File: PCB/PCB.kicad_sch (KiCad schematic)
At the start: 2 parts, among them U1 ESP32-DevKitC

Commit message: PCB progress
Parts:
- added BT1: Battery_Cell, Connector_PinHeader_2.54mm:PinHeader_1x02_P2.54mm_Vertical, symbol Device:Battery_Cell
- added D1: D, Diode_THT:D_A-405_P10.16mm_Horizontal, symbol Device:D
- added J1, J2, J3: Conn_01x04_Pin, Connector_PinHeader_2.54mm:PinHeader_1x04_P2.54mm_Vertical, symbol Connector:Conn_01x04_Pin
- added R1: 12k, Resistor_THT:R_Axial_DIN0207_L6.3mm_D2.5mm_P10.16mm_Horizontal, symbol Device:R
- added R2: 22k, Resistor_THT:R_Axial_DIN0207_L6.3mm_D2.5mm_P10.16mm_Horizontal, symbol Device:R
- added R3, R4, R5: 10k, Resistor_SMD:R_0402_1005Metric, symbol Device:R_Small
- added SW1: SW_SPDT, Connector_PinHeader_2.54mm:PinHeader_1x03_P2.54mm_Vertical, symbol Switch:SW_SPDT
- added SW2: SW_Push, Button_Switch_THT:SW_PUSH-12mm, symbol Switch:SW_Push
- added U2: ~, charging_module:TP4056-18650, symbol charging_module:charging_module
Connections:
- net +3.3V: now also DWM1.5 (VCC), J1.2 (Pin_2); no longer DWM1.15 (VCC)
- net CLK: now also DWM1.9 (SCK); no longer DWM1.23 (VSS)
- net CS: now also DWM1.12 (NSS); no longer DWM1.26 (NSS)
- net GND: now also DWM1.20 (GND), DWM1.6 (GND), DWM1.8 (GND), J1.1 (Pin_1), J3.4 (Pin_4), R2.2, SW2.1, U2.2 (GND), U2.3 (GND); no longer DWM1.16 (VSS), DWM1.22 (GND), DWM1.38 (GND)
- net MISO: now also DWM1.10 (MISO); no longer DWM1.24 (VSS)
- net MOSI: now also DWM1.11 (MOSI); no longer DWM1.25 (MOSI)
- net RST: now also DWM1.3 (~{RSTn}), U1.27 (GPIO16); no longer U1.29 (GPIO5)
- net at U1.19 (5V): now also SW1.3 (C)
- net IRQ: now reaches U1.28 (GPIO17)
- net IRQ: now also DWM1.7 (~{IRQn})
- net GPIO18: now reaches U1.30 (GPIO18)
- net GPIO18: now also J2.2 (Pin_2)
- net GPIO19: now reaches U1.31 (GPIO19)
- net GPIO19: now also J2.3 (Pin_3)
- net SDA: now reaches U1.33 (GPIO21)
- net SDA: now also J1.3 (Pin_3)
- net SCL: now reaches U1.36 (GPIO22)
- net SCL: now also J1.4 (Pin_4)
- net GPIO23: now reaches U1.37 (GPIO23)
- net GPIO23: now also J2.4 (Pin_4)
- net at U1.7 (32K_XP/GPIO32/ADC1_CH4): now also SW2.2
- net VBAT: now reaches U1.8 (32K_XN/GPIO33/ADC1_CH5)
- net VBAT: now also R1.2, R2.1
- new net: BT1.2 (-), U2.4 (B-)
- new net: BT1.1 (+), U2.5 (B+)
- new net: D1.2 (A), R1.1, U2.6 (VOUT)
- new net: DWM1.16 (VSS), R3.1
- new net: J3.1 (Pin_1), R3.2
- new net: J3.2 (Pin_2), R4.2
- new net: J3.3 (Pin_3), R5.2
- new net: DWM1.17 (GPIO2), R4.1
- new net: DWM1.19 (GPIO0), R5.1
- new net +5V: D1.1 (K), SW1.2 (B)
- new net GPIO5: J2.1 (Pin_1), U1.29 (GPIO5)
- now unconnected: DWM1.16 (VSS)
- no-connect marks 0 -> 9
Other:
- moved on the sheet: DWM1

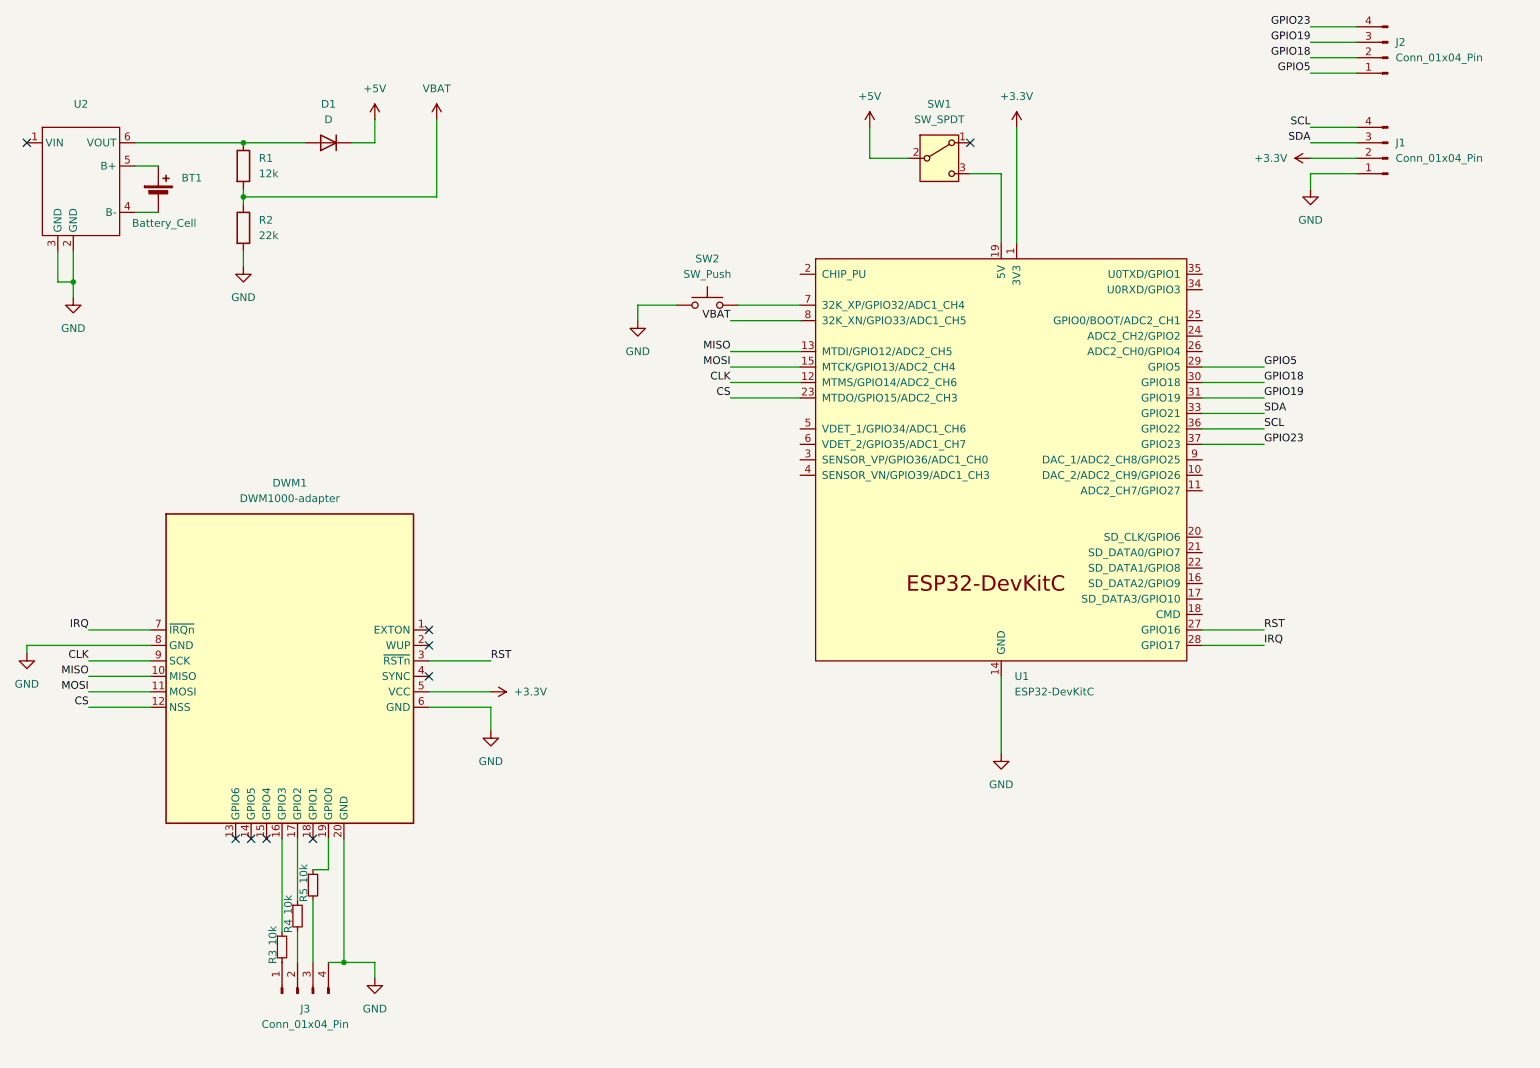
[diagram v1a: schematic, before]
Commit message: PCB is finished, but esp is the wrong way :(
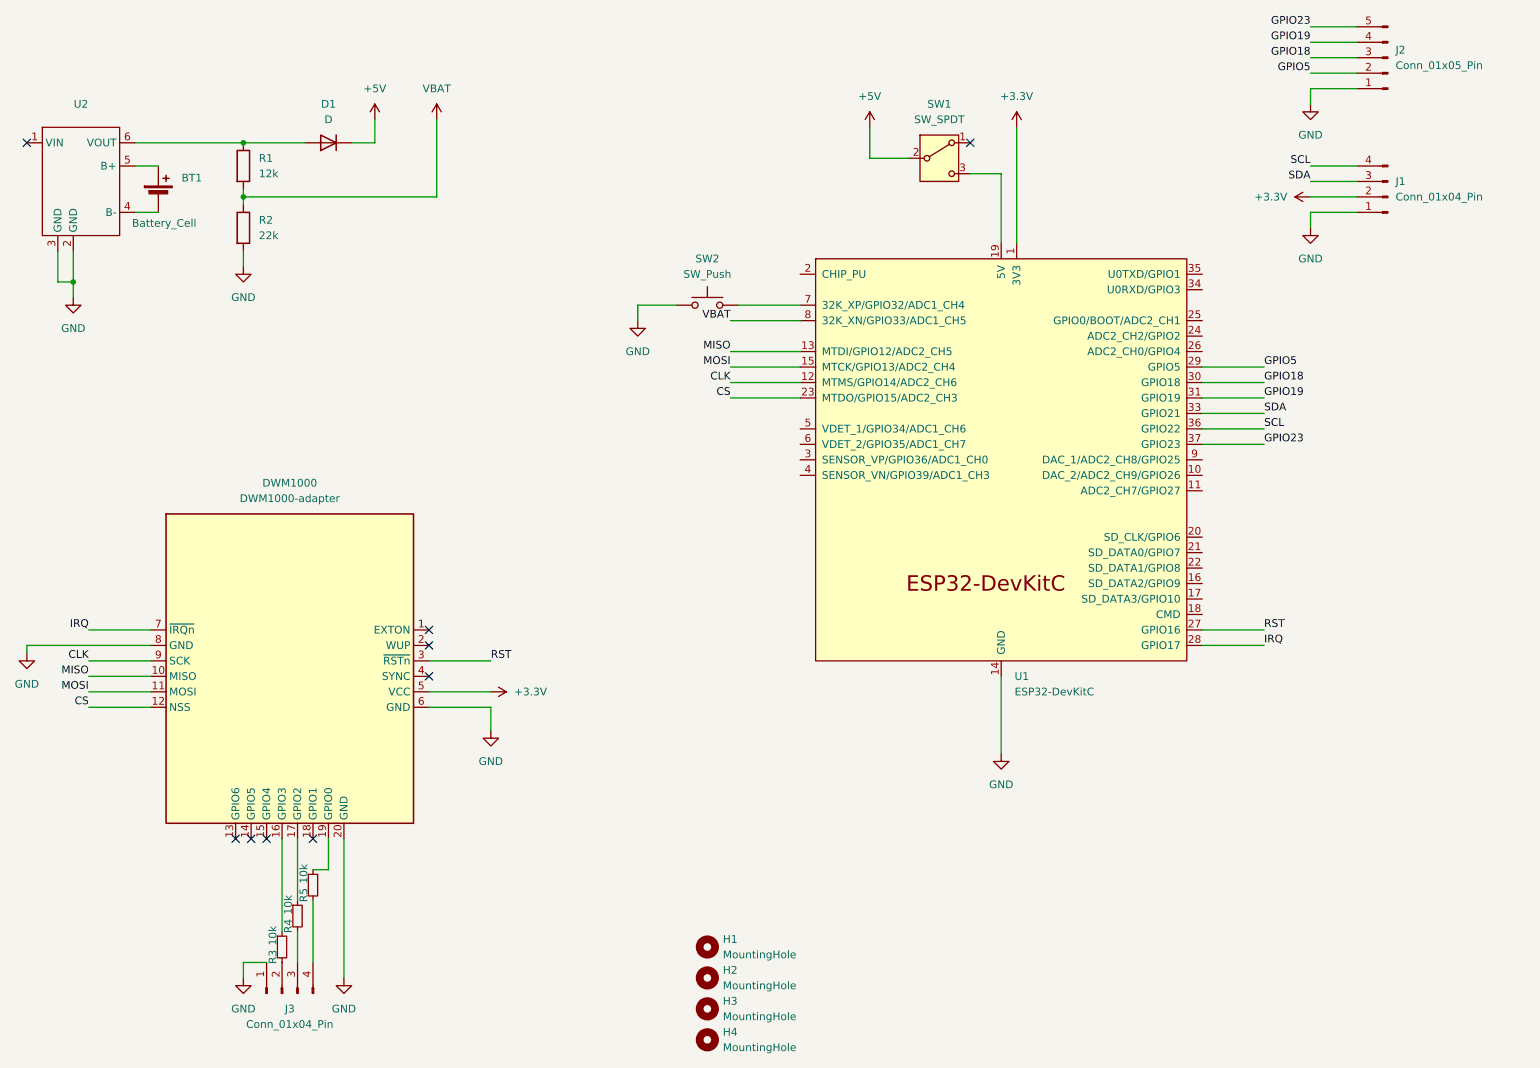
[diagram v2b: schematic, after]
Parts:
- removed J2: Conn_01x04_Pin, Connector_PinHeader_2.54mm:PinHeader_1x04_P2.54mm_Vertical, symbol Connector:Conn_01x04_Pin
- added H1, H2, H3, H4: MountingHole, MountingHole:MountingHole_4.3mm_M4, symbol Mechanical:MountingHole
- added J2: Conn_01x05_Pin, Connector_PinHeader_2.54mm:PinHeader_1x05_P2.54mm_Vertical, symbol Connector:Conn_01x05_Pin
- renumbered DWM1 to DWM1000
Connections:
- net GND: now also J3.1 (Pin_1), J2.1 (Pin_1); no longer J3.4 (Pin_4)
- net GPIO18: now also J2.3 (Pin_3)
- net GPIO19: now also J2.4 (Pin_4)
- net GPIO23: now also J2.5 (Pin_5)
- net GPIO5: now also J2.2 (Pin_2)
- net at R3.2: now also J3.2 (Pin_2); no longer J3.1 (Pin_1)
- net at R4.2: now also J3.3 (Pin_3); no longer J3.2 (Pin_2)
- net at R5.2: now also J3.4 (Pin_4); no longer J3.3 (Pin_3)
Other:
- moved on the sheet: J1, J3

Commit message: PCB redesign
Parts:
- H1, H2, H3, H4: footprint MountingHole:MountingHole_4.3mm_M4 -> MountingHole:MountingHole_3.2mm_M3
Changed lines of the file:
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@@
+	(wire
+		(pts
+			(xy 196.85 52.07) (xy 196.85 40.64)
+		)
+		(stroke
+			(width 0)
+			(type default)
+		)
+	)
 	(wire
 		(pts
@@
 	(wire
 		(pts
+			(xy 196.85 40.64) (xy 191.77 40.64)
+		)
+		(stroke
+			(width 0)
+			(type default)
+		)
+	)
+	(wire
+		(pts
 			(xy 72.39 35.56) (xy 82.55 35.56)
 		)
@@
 	(wire
 		(pts
-			(xy 196.85 40.64) (xy 196.85 52.07)
-		)
-		(stroke
-			(width 0)
-			(type default)
-		)
-	)
-	(wire
-		(pts
 			(xy 229.87 82.55) (xy 240.03 82.55)
 		)
@@
 		(pts
 			(xy 90.17 35.56) (xy 93.98 35.56)
-		)
-		(stroke
-			(width 0)
-			(type default)
-		)
-	)
-	(wire
-		(pts
-			(xy 191.77 40.64) (xy 196.85 40.64)
 		)
 		(stroke
@@
 			)
 		)
-		(property "Footprint" "MountingHole:MountingHole_4.3mm_M4"
+		(property "Footprint" "MountingHole:MountingHole_3.2mm_M3"
 			(at 148.59 177.8 0)
 			(effects
@@
 			)
 		)
-		(property "Footprint" "MountingHole:MountingHole_4.3mm_M4"
+		(property "Footprint" "MountingHole:MountingHole_3.2mm_M3"
 			(at 148.59 172.72 0)
 			(effects
@@
 			)
 		)
-		(property "Footprint" "MountingHole:MountingHole_4.3mm_M4"
+		(property "Footprint" "MountingHole:MountingHole_3.2mm_M3"
 			(at 148.59 182.88 0)
 			(effects
@@
 			)
 		)
-		(property "Footprint" "MountingHole:MountingHole_4.3mm_M4"
+		(property "Footprint" "MountingHole:MountingHole_3.2mm_M3"
 			(at 148.59 167.64 0)
 			(effects

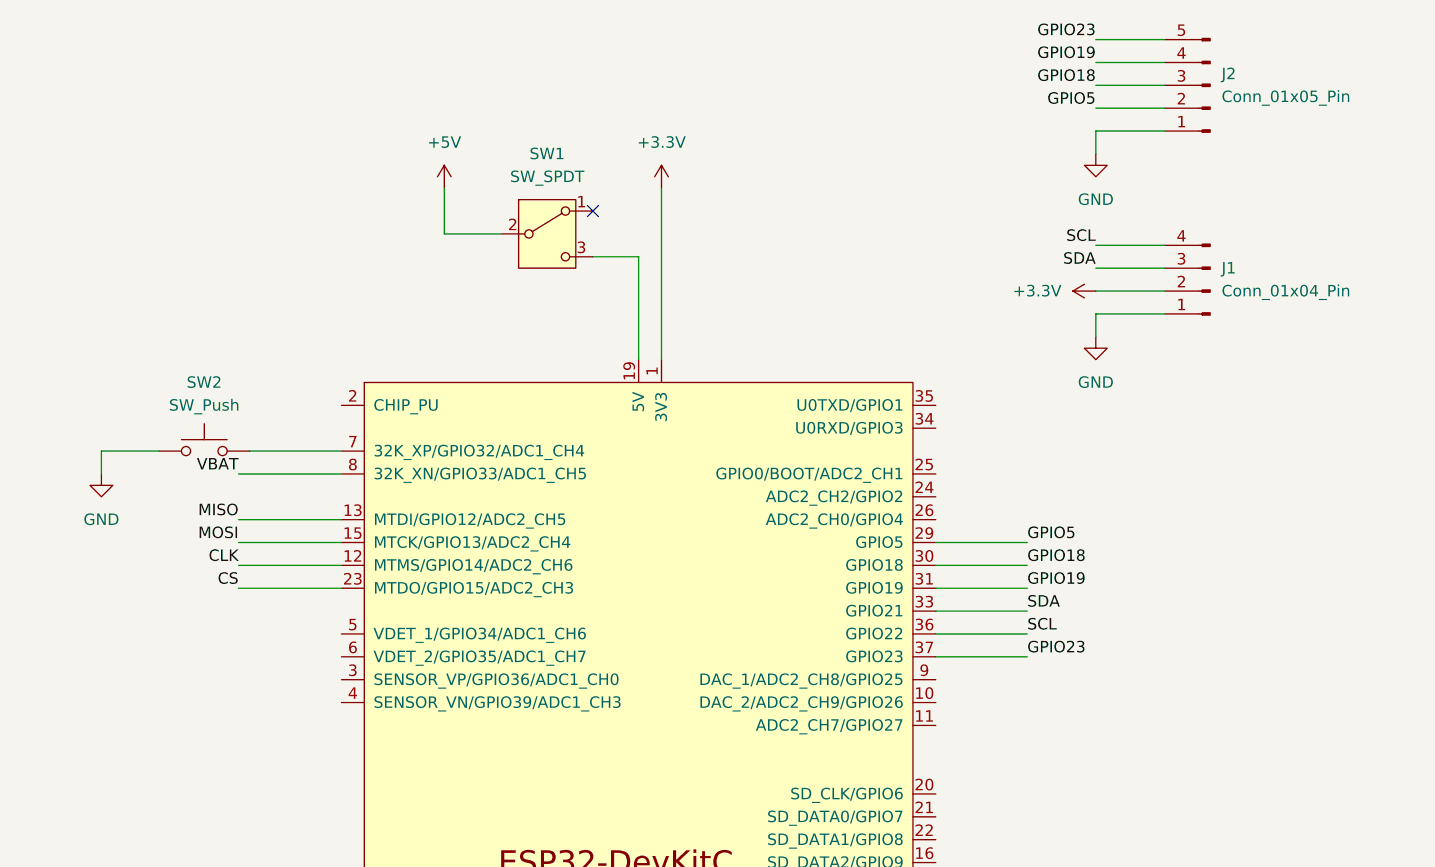
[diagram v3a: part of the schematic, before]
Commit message: added pins for motor encoders
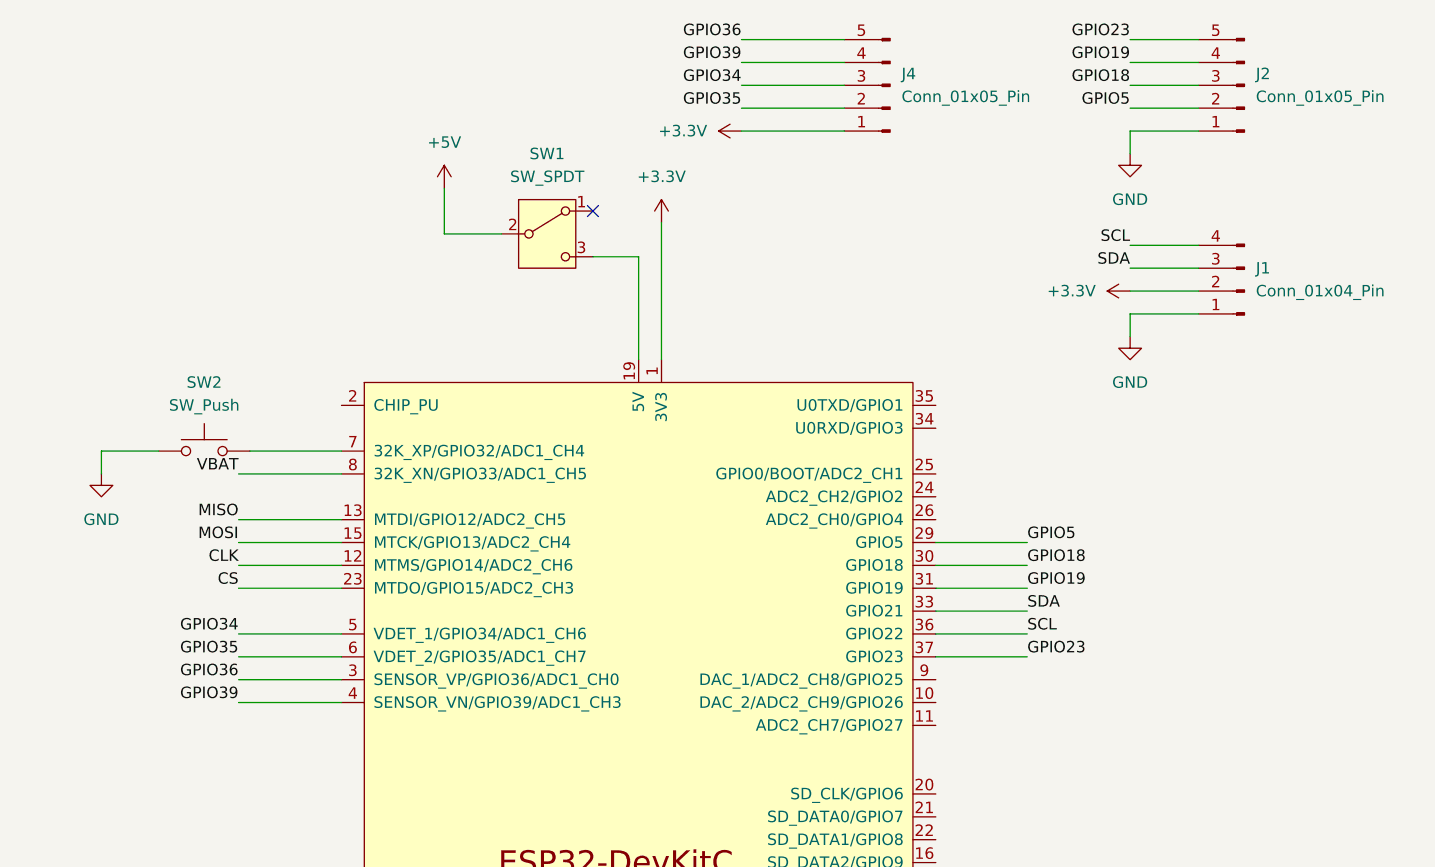
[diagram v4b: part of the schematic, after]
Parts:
- added J4: Conn_01x05_Pin, Connector_PinHeader_2.54mm:PinHeader_1x05_P2.54mm_Vertical, symbol Connector:Conn_01x05_Pin
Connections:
- net +3.3V: now also J4.1 (Pin_1)
- net GPIO36: now reaches U1.3 (SENSOR_VP/GPIO36/ADC1_CH0)
- net GPIO36: now also J4.5 (Pin_5)
- net GPIO39: now reaches U1.4 (SENSOR_VN/GPIO39/ADC1_CH3)
- net GPIO39: now also J4.4 (Pin_4)
- net GPIO34: now reaches U1.5 (VDET_1/GPIO34/ADC1_CH6)
- net GPIO34: now also J4.3 (Pin_3)
- net GPIO35: now reaches U1.6 (VDET_2/GPIO35/ADC1_CH7)
- net GPIO35: now also J4.2 (Pin_2)
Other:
- moved on the sheet: J1, J2

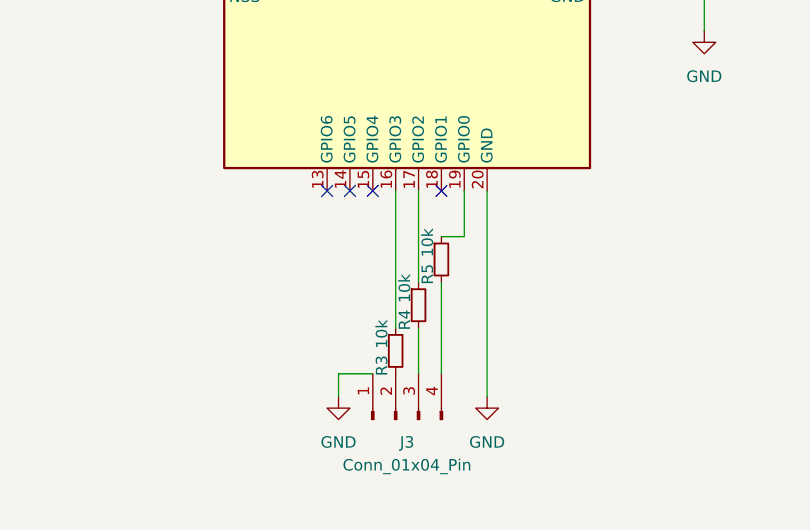
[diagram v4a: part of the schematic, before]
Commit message: new header for encoders, adjusted resitor values
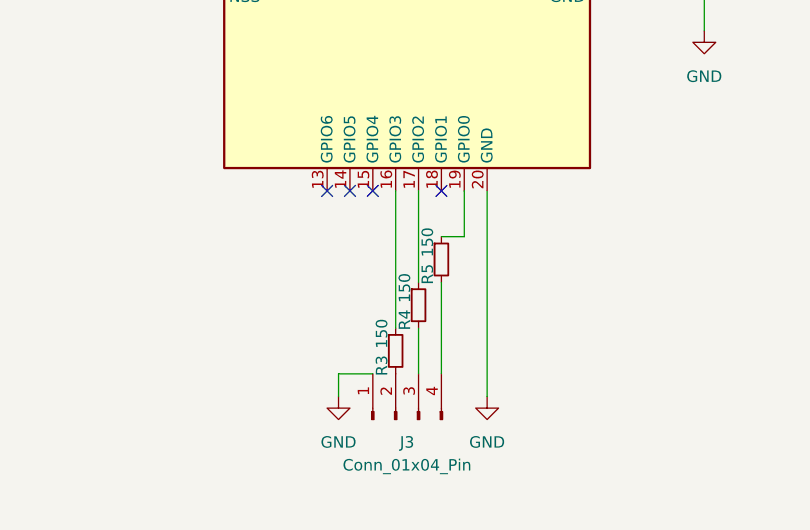
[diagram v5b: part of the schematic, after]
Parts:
- R3, R4, R5: value 10k -> 150
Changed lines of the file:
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@@
 			)
 		)
-		(property "Value" "10k"
+		(property "Value" "150"
 			(at 77.216 167.386 90)
 			(effects
@@
 			)
 		)
-		(property "Value" "10k"
+		(property "Value" "150"
 			(at 79.756 162.306 90)
 			(effects
@@
 			)
 		)
-		(property "Value" "10k"
+		(property "Value" "150"
 			(at 82.296 157.226 90)
 			(effects

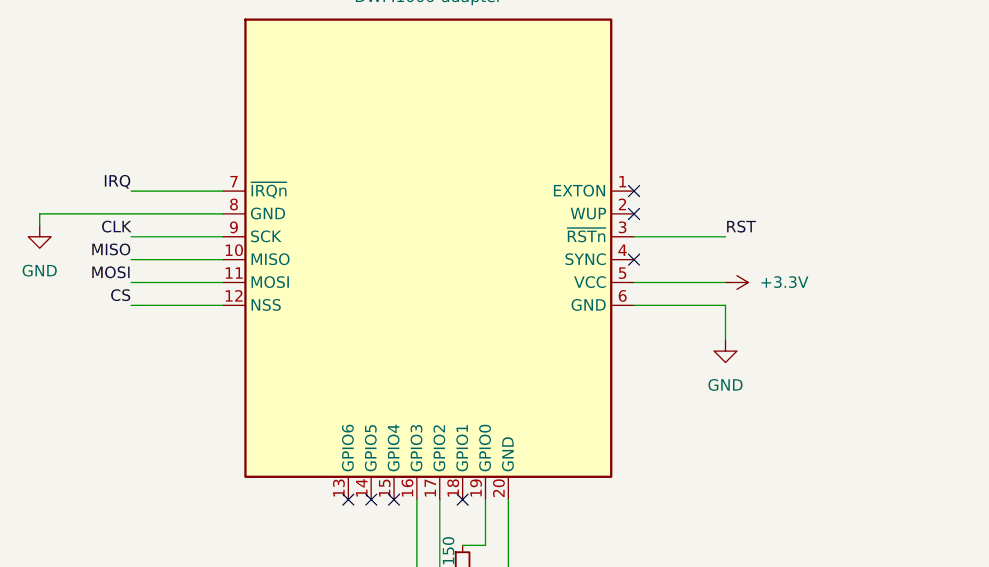
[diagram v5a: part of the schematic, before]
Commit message: fix: fixed wrong wiring of the UWB
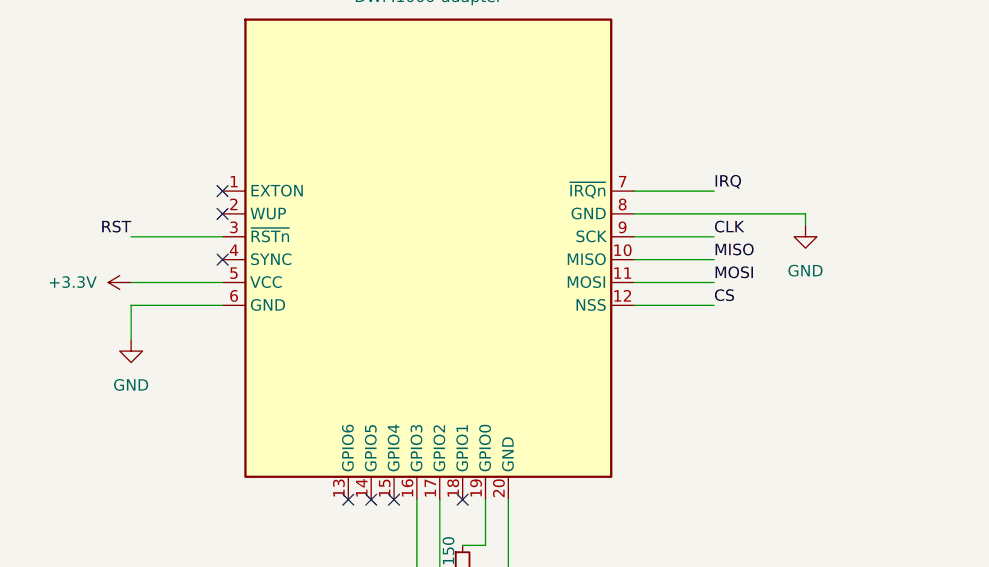
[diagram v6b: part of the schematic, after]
